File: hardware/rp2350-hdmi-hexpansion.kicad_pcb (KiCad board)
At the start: 2 copper layers, 32 x 36.6 mm, 7 parts, among them J1 Nodule-Connector, J2 Conn_02x10_Odd_Even

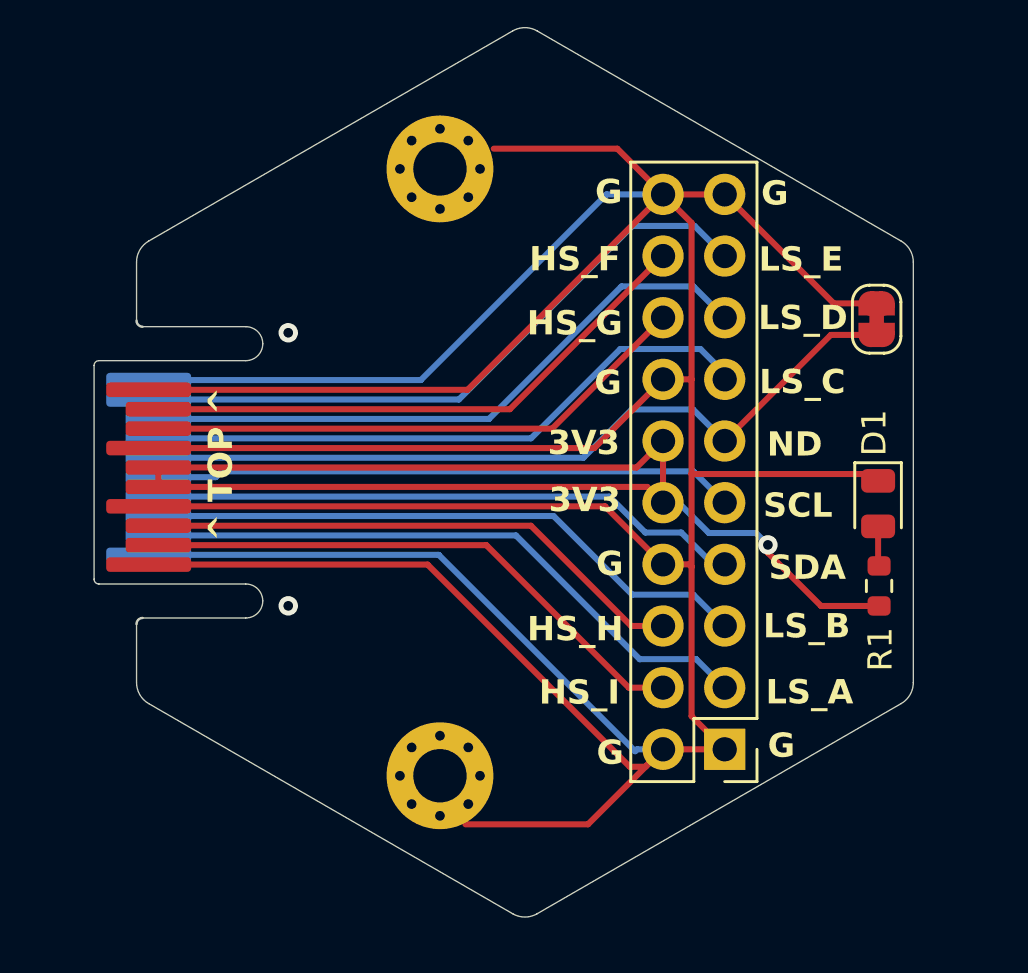
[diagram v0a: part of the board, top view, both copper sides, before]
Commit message: hardware: upgrade KiCad project to KiCad 10, remove J2, ignore local clutter
Re-saved schematic/PCB/project in KiCad 10 (file format upgrade) and
removed J2 from the schematic and board. Add a hardware/.gitignore for
KiCad's local history, backup zips and lock files.

Co-Authored-By: Claude Opus 5.5 <noreply@anthropic.com>
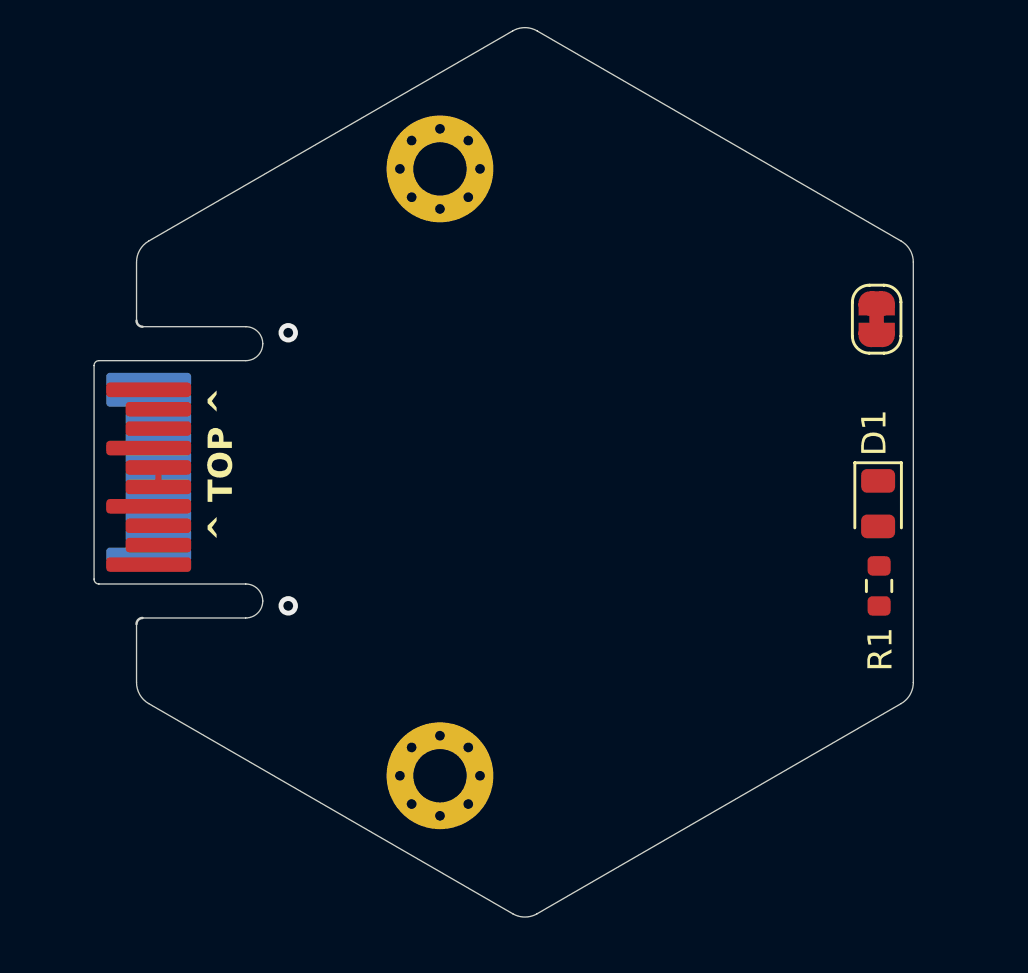
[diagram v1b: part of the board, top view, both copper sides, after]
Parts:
- removed J2: Conn_02x10_Odd_Even, Connector_PinHeader_2.54mm:PinHeader_2x10_P2.54mm_Vertical
- J1: value Nodule-Connector -> Hexpansion-Connector
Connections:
- J1 pad 2: /LS_A -> unconnected-(J1-LS_A-Pad2)
- J1 pad 3: /LS_B -> unconnected-(J1-LS_B-Pad3)
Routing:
- net /GND: track 207.4 -> 0.00 mm
- net /3V3: track 56.5 -> 0.80 mm, vias 1 -> 0
- net /HEXP_DET: track 32.8 -> 0.00 mm
- net /LS_E: track 27.2 -> 0.00 mm
- net /LS_D: track 26.1 -> 0.00 mm
- net /LS_A: track 25.9 -> 0.00 mm
- net /LS_C: track 25.5 -> 0.00 mm
- net /LS_B: track 25.2 -> 0.00 mm
- net /SDA: track 24.5 -> 0.00 mm
- net /SCL: track 24.0 -> 0.00 mm
- net /HS_F: track 23.4 -> 0.00 mm
- net /HS_I: track 23.2 -> 0.00 mm
- net /HS_G: track 22.7 -> 0.00 mm
- net /HS_H: track 22.5 -> 0.00 mm
- net Net-(D1-A): track 1.64 -> 0.00 mm
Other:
- copper layers 2 -> 4
- board text removed: "3V3"
- board text removed: "G"
- board text removed: "HS_F"
- board text removed: "HS_G"
- board text removed: "HS_H"
- board text removed: "HS_I"
- board text removed: "LS_A"
- board text removed: "LS_B"
- board text removed: "LS_C"
- board text removed: "LS_D"
- board text removed: "LS_E"
- board text removed: "ND"
- board text removed: "SCL"
- board text removed: "SDA"

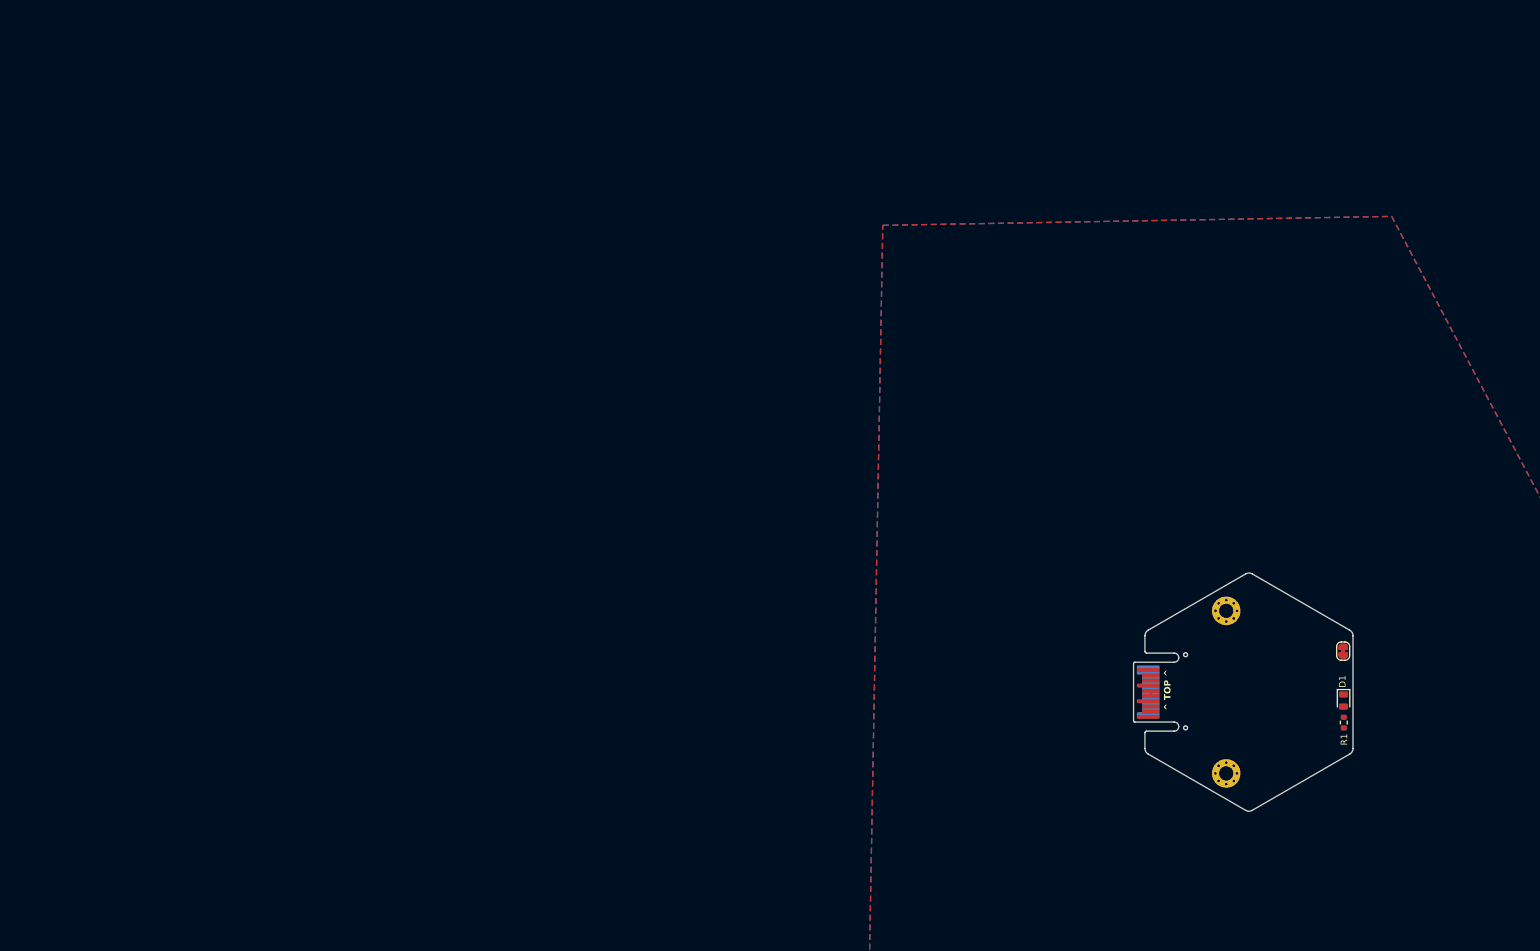
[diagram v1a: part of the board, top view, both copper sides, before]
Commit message: hardware: edge connector back to J1 and locked in place, HDMI now J5
- Schematic: hexpansion edge connector is J1 again (same symbol UUID as
  the J1 footprint already on the PCB, so Update PCB keeps its position);
  HDMI Type A socket renumbered J1 -> J5. ERC and netlist re-verified.
- PCB: J1 edge connector footprint locked at x 98.25, y 100 mm, F.Cu, so
  layout work can't move it accidentally. Position confirmed unchanged.
- BOMs regenerated for the new references; HISTORY lists the connector
  numbering.

Co-Authored-By: Claude Opus 5.5 <noreply@anthropic.com>
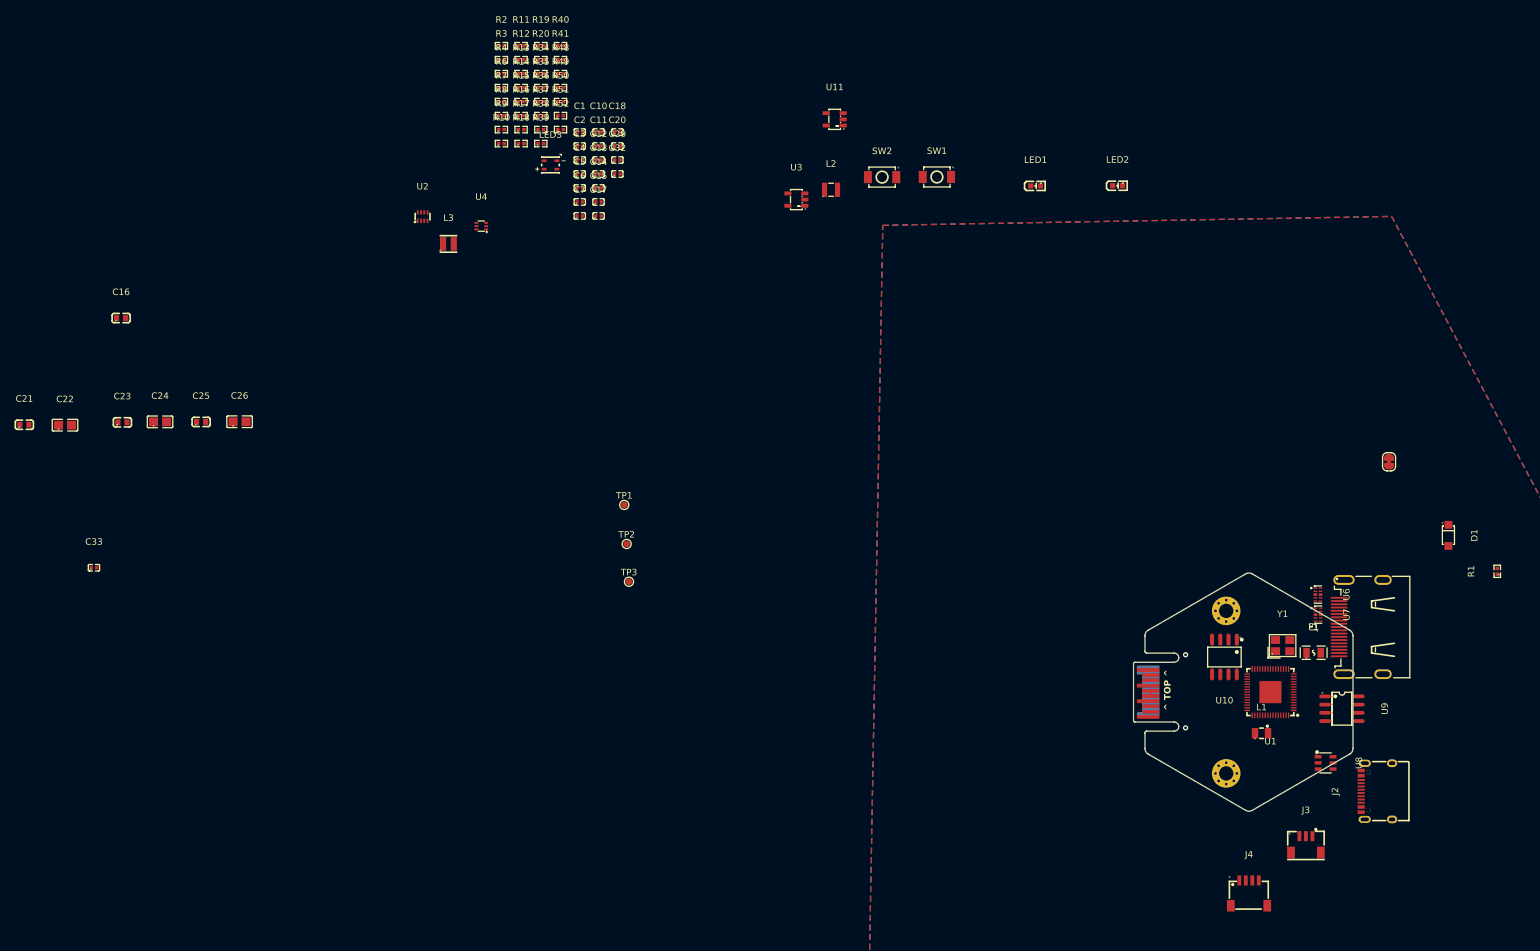
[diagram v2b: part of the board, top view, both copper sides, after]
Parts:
- added C1: 100nF, jlc:C0402, F.Cu at (13.1, 13.9)
- added C10: 100nF, jlc:C0402, F.Cu at (16.0, 13.9)
- added C11: 100nF, jlc:C0402, F.Cu at (16.0, 16.0)
- added C12: 100nF, jlc:C0402, F.Cu at (16.0, 18.2)
- added C13: 4.7uF, jlc:C0402, F.Cu at (16.0, 20.3)
- added C14: 4.7uF, jlc:C0402, F.Cu at (16.0, 22.5)
- added C15: 4.7uF, jlc:C0402, F.Cu at (16.0, 24.6)
- added C16: 10uF, jlc:C0603, F.Cu at (-57.5, 42.5)
- added C17: 15pF, jlc:C0402, F.Cu at (16.0, 26.8)
- added C18: 15pF, jlc:C0402, F.Cu at (18.8, 13.9)
- added C2: 100nF, jlc:C0402, F.Cu at (13.1, 16.0)
- added C20: 100nF, jlc:C0402, F.Cu at (18.8, 16.0)
- added C21: 10uF, jlc:C0603, F.Cu at (-72.4, 58.9)
- added C22: 22uF, jlc:C0805, F.Cu at (-66.1, 58.9)
- added C23: 10uF, jlc:C0603, F.Cu at (-57.3, 58.5)
- added C24: 22uF, jlc:C0805, F.Cu at (-51.5, 58.4)
- added C25: 10uF, jlc:C0603, F.Cu at (-45.2, 58.4)
- added C26: 22uF, jlc:C0805, F.Cu at (-39.3, 58.4)
- added C29: 100nF, jlc:C0402, F.Cu at (18.8, 18.2)
- added C3: 100nF, jlc:C0402, F.Cu at (13.1, 18.2)
- added C32: 100nF, jlc:C0402, F.Cu at (18.8, 20.3)
- added C33: 100nF, jlc:C0402, F.Cu at (-61.7, 80.9)
- added C4: 100nF, jlc:C0402, F.Cu at (13.1, 20.3)
- added C5: 100nF, jlc:C0402, F.Cu at (13.1, 22.5)
- added C6: 100nF, jlc:C0402, F.Cu at (13.1, 24.6)
- added C7: 100nF, jlc:C0402, F.Cu at (13.1, 26.8)
- added F1: 200mA PTC, jlc:F0805, F.Cu at (126.0, 93.9)
- added J2: USB-C, jlc:USB-C-SMD_TYPE-C-16PIN-2MD-073, F.Cu at (135.6, 115.3)
- added J3: SWD, jlc:CONN-SMD-3P-P1.00_BM03B-SRSS-TB-LF-SN, F.Cu at (124.8, 123.4)
- added J4: Qwiic, jlc:CONN-SMD_4P-P1.00_SM04B-SRSS-TB-LF-SN, F.Cu at (116.0, 130.9)
- added J5: HDMI-A, jlc:HDMI-SMD_19P-P0.50-H-F, F.Cu at (133.2, 90.0)
- added L1: 3.3uH, jlc:IND-SMD_L2.0-W1.6_AOTA-B201610S3R3-101-T, F.Cu at (117.9, 106.3)
- added L2: 2.2uH, jlc:IND-SMD_L2.5-W2.0_MHCHL2520, F.Cu at (51.7, 22.7)
- added L3: 1uH, jlc:IND-SMD_L2.5-W2.0_FTC252010S, F.Cu at (-7.13, 31.1)
- added LED1: PWR, jlc:LED-SMD_L1.6-W0.8-R-RD, F.Cu at (83.2, 22.1)
- added LED2: STATUS, jlc:LED-SMD_L1.6-W0.8-R-RD, F.Cu at (95.8, 22.1)
- added LED3: SK6805, jlc:LED-SMD_4P-L2.7-W2.4_SK6805MICRO-J, F.Cu at (8.56, 18.9)
- added R10: 27R, jlc:R0402, F.Cu at (1.01, 15.6)
- added R11: 27R, jlc:R0402, F.Cu at (4.04, 0.57)
- added R12: 100k, jlc:R0402, F.Cu at (4.04, 2.73)
- added R13: 22k, jlc:R0402, F.Cu at (4.04, 4.88)
- added R14: 33k, jlc:R0402, F.Cu at (4.04, 7.03)
- added R15: 22k, jlc:R0402, F.Cu at (4.04, 9.18)
- added R16: 100k, jlc:R0402, F.Cu at (4.04, 11.3)
- added R17: 100k, jlc:R0402, F.Cu at (4.04, 13.5)
- added R18: 100k, jlc:R0402, F.Cu at (4.04, 15.6)
- added R19: 200k, jlc:R0402, F.Cu at (7.08, 0.57)
- added R2: 1k, jlc:R0402, F.Cu at (1.01, 0.57)
- added R20: 27k, jlc:R0402, F.Cu at (7.08, 2.73)
- added R3: 10k, jlc:R0402, F.Cu at (1.01, 2.73)
- added R34: 100k, jlc:R0402, F.Cu at (7.08, 4.88)
- added R35: 100k, jlc:R0402, F.Cu at (7.08, 7.03)
- added R36: 33R, jlc:R0402, F.Cu at (7.08, 9.18)
- added R37: 33R, jlc:R0402, F.Cu at (7.08, 11.3)
- added R38: 33R, jlc:R0402, F.Cu at (7.08, 13.5)
- added R39: 33R, jlc:R0402, F.Cu at (7.08, 15.6)
- added R4: 10k, jlc:R0402, F.Cu at (1.01, 4.88)
- added R40: 1k, jlc:R0402, F.Cu at (10.1, 0.57)
- added R41: 10k, jlc:R0402, F.Cu at (10.1, 2.73)
- added R48: 4.7k, jlc:R0402, F.Cu at (10.1, 4.88)
- added R49: 4.7k, jlc:R0402, F.Cu at (10.1, 7.03)
- added R50: 4.7k, jlc:R0402, F.Cu at (10.1, 9.18)
- added R51: 1k, jlc:R0402, F.Cu at (10.1, 11.3)
- added R52: 330R, jlc:R0402, F.Cu at (10.1, 13.5)
- added R6: 1k, jlc:R0402, F.Cu at (1.01, 7.03)
- added R7: 10k, jlc:R0402, F.Cu at (1.01, 9.18)
- added R8: 5.1k, jlc:R0402, F.Cu at (1.01, 11.3)
- added R9: 5.1k, jlc:R0402, F.Cu at (1.01, 13.5)
- added SW1: BOOTSEL, jlc:SW-SMD_L3.9-W3.0-P4.45, F.Cu at (68.0, 20.8)
- added SW2: RESET, jlc:SW-SMD_L3.9-W3.0-P4.45, F.Cu at (59.6, 20.8)
- added TP1: +3V3, TestPoint:TestPoint_Pad_D1.0mm, F.Cu at (19.9, 71.2)
- added TP2: V5_HDMI, TestPoint:TestPoint_Pad_D1.0mm, F.Cu at (20.3, 77.2)
- added TP3: GND, TestPoint:TestPoint_Pad_D1.0mm, F.Cu at (20.6, 83.0)
- added U1: RP2354A, jlc:QFN-60_L7.0-W7.0-P0.40-TL-EP3.4, F.Cu at (119.3, 100.0)
- added U10: ZD24C64A (fallback), jlc:SOP-8_L4.9-W3.9-P1.27-LS6.0-BL, F.Cu at (112.2, 94.6)
- added U11: SN74LVC1G07, jlc:SOT-23-5_L3.0-W1.7-P0.95-LS2.8-BR, F.Cu at (52.3, 11.9)
- added U2: TPS2116DRLR, jlc:SOT-583-8_L2.1-W1.6-P0.50-LS1.6-BL, F.Cu at (-11.1, 26.9)
- added U3: TLV62569DBVR, jlc:SOT-23-5_L3.0-W1.7-P0.95-LS2.8-BR, F.Cu at (46.4, 24.2)
- added U4: TPS61023DRLR, jlc:SOT-563_L1.6-W1.2-P0.50-LS1.6-BR, F.Cu at (-2.08, 28.3)
- added U6: TPD4E05U06, jlc:USON-10_L2.5-W1.0-P0.50-BL, F.Cu at (126.6, 85.0)
- added U7: TPD4E05U06, jlc:USON-10_L2.5-W1.0-P0.50-BL, F.Cu at (126.6, 88.1)
- added U8: USBLC6-2SC6, jlc:SOT-23-6_L2.9-W1.6-P0.95-LS2.8-BL, F.Cu at (127.8, 110.9)
- added U9: APS6404L-3SQR-SN, jlc:SOIC-8_L4.9-W3.9-P1.27-LS6.0-BL, F.Cu at (130.3, 102.5)
- added Y1: 12MHz, jlc:CRYSTAL-SMD_4P-L3.2-W2.5-BL, F.Cu at (121.2, 92.8)
- D1: value LED -> SMF5.0A; footprint LED_SMD:LED_0805_2012Metric -> jlc:SOD-123FL_L2.7-W1.8-LS3.8-RD
- H1, H2: value MountingHole_Pad -> MountingHole
- JP1: value SolderJumper_2_Bridged -> Qwiic pull-ups
- R1: value R -> 33R; footprint Resistor_SMD:R_0603_1608Metric -> jlc:R0402
- moved R1 33.1 mm to (154.2, 81.4)
- moved D1 30.1 mm to (146.7, 75.9)
- moved JP1 30.0 mm to (137.6, 64.6)
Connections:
- D1 pad 1: /GND -> /VBUS
- D1 pad 2: Net-(D1-A) -> /GND
- J1 pad 15: /3V3 -> /3V3_BADGE
- J1 pad 16: /3V3 -> /3V3_BADGE
- J1 pad 2: unconnected-(J1-LS_A-Pad2) -> /LS_A
- J1 pad 3: unconnected-(J1-LS_B-Pad3) -> /LS_B
- J1 pad 4: /SDA -> /BADGE_SDA
- J1 pad 5: /SCL -> /BADGE_SCL
- J1 pad 6: /HEXP_DET -> /GND
- J1 pad 7: /LS_C -> unconnected-(J1-LS_C-Pad7)
- J1 pad 8: /LS_D -> unconnected-(J1-LS_D-Pad8)
- J1 pad 9: /LS_E -> unconnected-(J1-LS_E-Pad9)
- JP1 pad 1: /HEXP_DET -> /+3V3
- JP1 pad 2: /GND -> /QWIIC_PU
- R1 pad 1: /3V3 -> /+3V3
- R1 pad 2: Net-(D1-A) -> /VREG_AVDD
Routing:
- net /3V3_BADGE: track 0.00 -> 0.80 mm
- net /3V3: track 0.80 -> 0.00 mm

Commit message: hardware: lock mounting holes, KiCad 10 re-save, early placement
- PCB: H1 (112.5, 112.5) and H2 (112.5, 87.5) mounting holes locked,
  alongside the J1 edge connector. All footprint positions verified
  unchanged by the lock edit.
- PCB: D1 (VBUS TVS) and R1 (VREG_AVDD filter) moved during initial
  placement.
- Schematic re-saved by KiCad 10 (format only; netlist re-verified,
  344 pins match, ERC unchanged). Project schematic revision set to 0.1.

Co-Authored-By: Claude Opus 5.5 <noreply@anthropic.com>
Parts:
- moved R1 45.8 mm to (114.7, 104.7), turned to 0 degrees
- moved D1 40.5 mm to (151.0, 116.1), turned to 0 degrees
